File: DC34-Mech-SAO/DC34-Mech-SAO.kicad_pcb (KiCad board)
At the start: 2 copper layers, 27.9 x 38 mm, 20 parts, among them J1 Conn_01x06_Male, J2 Conn_01x03_Male, U1 ATtiny816-M

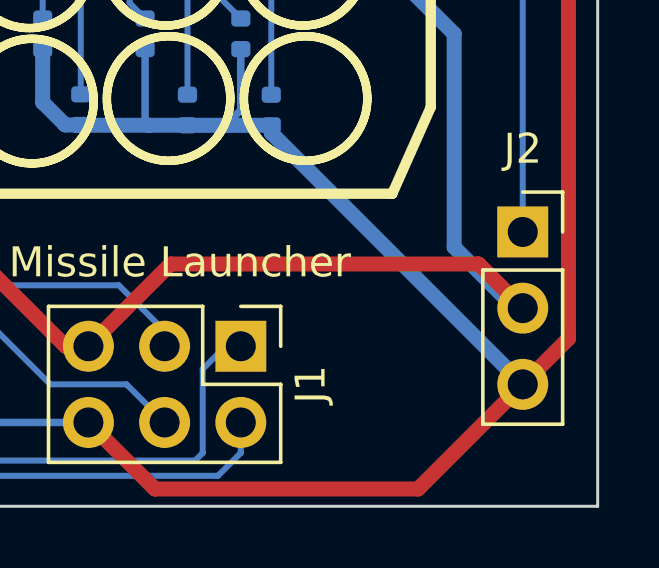
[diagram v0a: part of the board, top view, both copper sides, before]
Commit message: Added silkscreen
Added descriptive text to board.
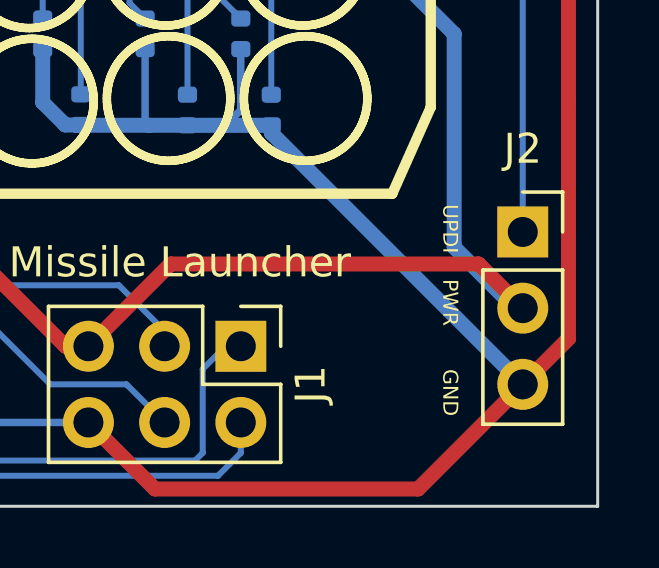
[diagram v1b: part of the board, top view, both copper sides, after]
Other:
- board text added: "Designed by CPEC in Arizona Manufactured in China"
- board text added: "GND"
- board text added: "Mech Fighters SAO Rev 1"
- board text added: "PWR"
- board text added: "UPDI"
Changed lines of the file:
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@@
 		(layer "Edge.Cuts")
+	)
+	(gr_text "UPDI"
+		(at 153.5 90 270)
+		(layer "F.SilkS")
+		(effects
+			(font
+				(size 0.5 0.5)
+				(thickness 0.07)
+			)
+			(justify left bottom)
+		)
+	)
+	(gr_text "PWR"
+		(at 153.5 92.5 270)
+		(layer "F.SilkS")
+		(effects
+			(font
+				(size 0.5 0.5)
+				(thickness 0.07)
+			)
+			(justify left bottom)
+		)
+	)
+	(gr_text "GND"
+		(at 153.5 95.5 270)
+		(layer "F.SilkS")
+		(effects
+			(font
+				(size 0.5 0.5)
+				(thickness 0.07)
+			)
+			(justify left bottom)
+		)
 	)
 	(gr_text "Missile Launcher"
@@
 		)
 	)
+	(gr_text "Mech Fighters SAO Rev 1"
+		(at 153.5 81 0)
+		(layer "B.SilkS")
+		(effects
+			(font
+				(size 1 1)
+				(thickness 0.15)
+			)
+			(justify left bottom mirror)
+		)
+	)
+	(gr_text "Designed by CPEC in Arizona\nManufactured in China"
+		(at 143 92 0)
+		(layer "B.SilkS")
+		(effects
+			(font
+				(size 1 1)
+				(thickness 0.15)
+			)
+			(justify bottom mirror)
+		)
+	)
